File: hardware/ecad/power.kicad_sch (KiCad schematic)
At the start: 18 parts, among them J1 Conn_01x02, U1 TPS62162DSG, U2 BQ24079RGTT

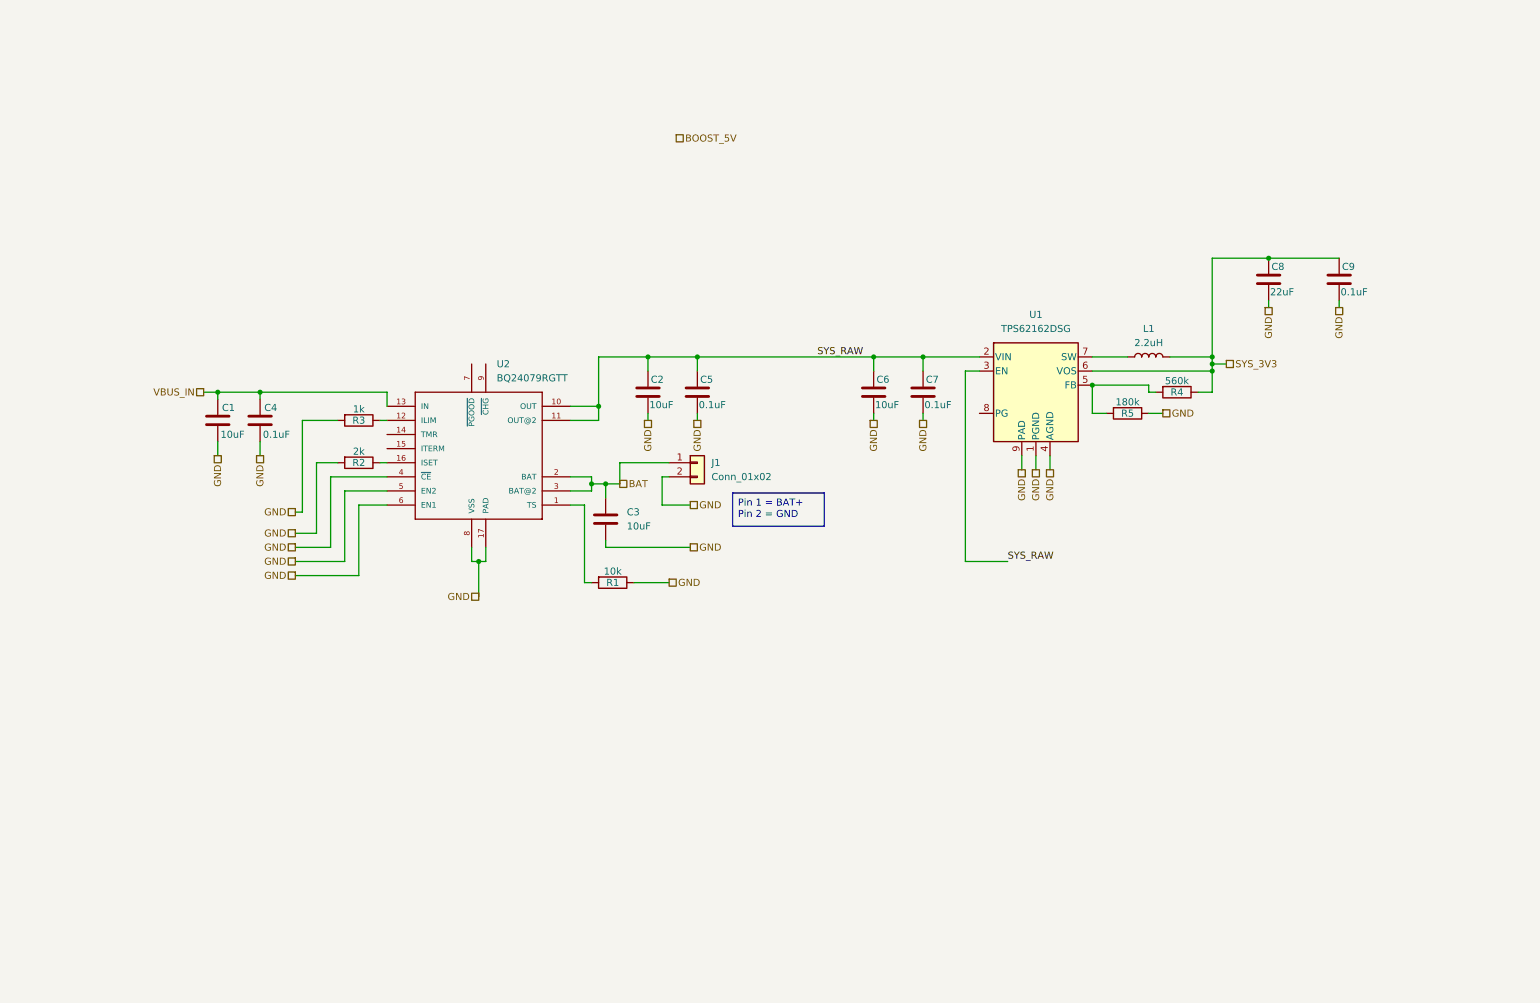
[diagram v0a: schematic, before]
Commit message: Power schematic finished, top level schematic editied to swap from I2c to SPI instead
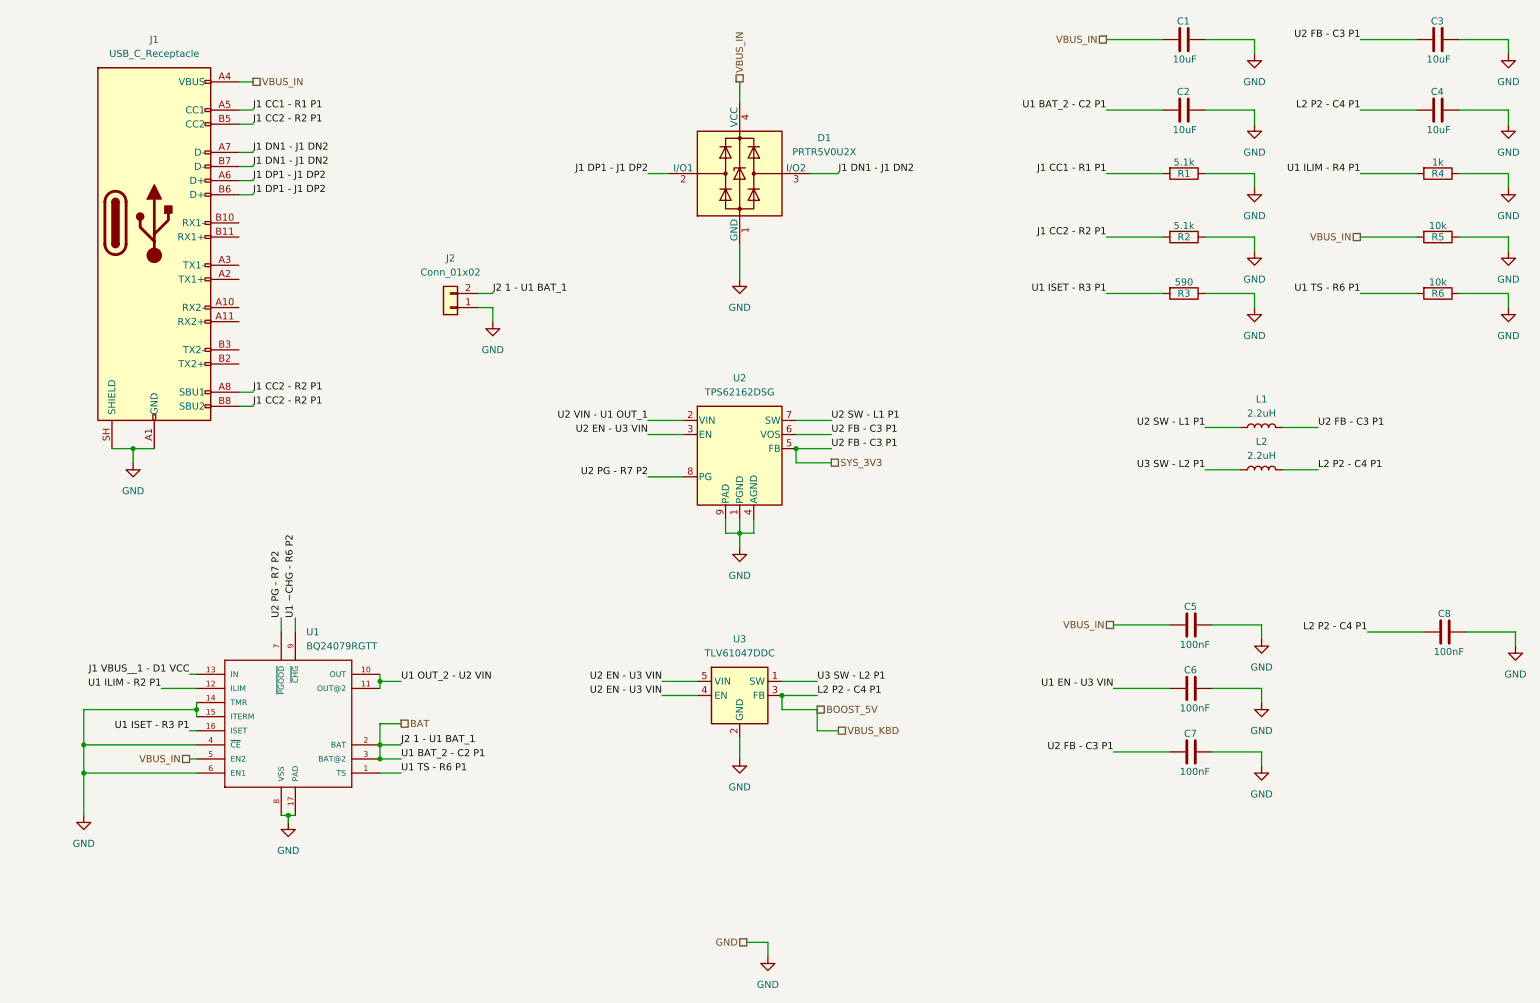
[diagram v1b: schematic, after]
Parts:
- removed C9: 0.1uF, Capacitor_SMD:C_0603_1608Metric, symbol Device:C
- removed J1: Conn_01x02, Connector_JST:JST_PH_B2B-PH-K_1x02_P2.00mm_Vertical, symbol Connector_Generic:Conn_01x02
- removed U1: TPS62162DSG, Package_SON:WSON-8-1EP_2x2mm_P0.5mm_EP0.9x1.6mm_ThermalVias, symbol Regulator_Switching:TPS62162DSG
- removed U2: BQ24079RGTT, footprints:QFN50P400X400X80-17N, symbol BQ24074RGTT:BQ24074RGTT
- added D1: PRTR5V0U2X, Package_TO_SOT_SMD:SOT-143, symbol Power_Protection:PRTR5V0U2X
- added J1: USB_C_Receptacle, Connector_USB:USB_C_Receptacle_Amphenol_12401610E4-2A_CircularHoles, symbol Connector:USB_C_Receptacle
- added J2: Conn_01x02, Connector_JST:JST_PH_B2B-PH-K_1x02_P2.00mm_Vertical, symbol Connector_Generic:Conn_01x02
- added L2: 2.2uH, Inductor_SMD:L_0603_1608Metric, symbol Device:L
- added R6: 10k, Resistor_SMD:R_0201_0603Metric, symbol Device:R
- added U1: BQ24079RGTT, footprints:QFN50P400X400X80-17N, symbol BQ24074RGTT:BQ24074RGTT
- added U2: TPS62162DSG, Package_SON:WSON-8-1EP_2x2mm_P0.5mm_EP0.9x1.6mm_ThermalVias, symbol Regulator_Switching:TPS62162DSG
- added U3: TLV61047DDC, Package_TO_SOT_SMD:SOT-23-5, symbol Regulator_Switching:TLV61047DDC
- C4: value 0.1uF -> 10uF
- C5, C7: value 0.1uF -> 100nF
- C6: value 10uF -> 100nF
- C8: value 22uF -> 100nF
- R1: value 10k -> 5.1k
- R2: value 2k -> 5.1k
- R3: value 1k -> 590
- R4: value 560k -> 1k
- R5: value 180k -> 10k
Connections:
- net SYS_RAW is gone; now on net GND: C2.1, C5.1, C6.1, C7.1
- net BAT: now also C2.2, J2.2 (Pin_2), U1.2 (BAT), U1.3 (BAT@2); no longer C3.1
- net BOOST_5V: now also C4.2, C8.2, L2.2, U3.3 (FB)
- net GND: now also C1.1, C3.1, C4.1, C8.1, R2.1, R3.1, R4.1, D1.1 (GND), J1.A1 (GND), J1.A12 (GND), J1.B1 (GND), J1.B12 (GND), J1.SH (SHIELD), J2.1 (Pin_1), R6.1, U1.14 (TMR), U1.15 (ITERM), U1.17 (PAD), U1.4 (~{CE}), U1.6 (EN1), U1.8 (VSS), U2.1 (PGND), U2.4 (AGND), U2.9 (PAD), U3.2 (GND); no longer C1.2, C2.2, C3.2, C4.2, C5.2, C6.2, C7.2, C8.2, R2.2, R3.2
- net SYS_3V3: now also C3.2, C7.2, U2.5 (FB), U2.6 (VOS); no longer C8.1, R4.1
- net VBUS_IN: now also C1.2, C5.2, R5.2, D1.4 (VCC), J1.A4 (VBUS), J1.A9 (VBUS), J1.B4 (VBUS), J1.B9 (VBUS), U1.5 (EN2); no longer C1.1, C4.1
- net J1 CC1 - R1 P1: now reaches R1.2
- net J1 CC1 - R1 P1: now also J1.A5 (CC1)
- net U1 ILIM - R4 P1: now reaches R4.2
- net U1 ILIM - R4 P1: no longer R5.2
- net U2 SW - L1 P1: now reaches L1.1
- net U2 SW - L1 P1: now also U2.7 (SW)
- new net J1 CC2 - R2 P1: J1.A8 (SBU1), J1.B5 (CC2), J1.B8 (SBU2), R2.2
- new net J1 DN1 - J1 DN2: D1.3 (I/O2), J1.A7 (D-), J1.B7 (D-)
- new net J1 DP1 - J1 DP2: D1.2 (I/O1), J1.A6 (D+), J1.B6 (D+)
- new net J1 VBUS__1 - D1 VCC: U1.13 (IN)
- new net U1 EN - U3 VIN: C6.2
- new net U1 ILIM - R2 P1: U1.12 (ILIM)
- new net U1 ISET - R3 P1: R3.2, U1.16 (ISET)
- new net U1 OUT_2 - U2 VIN: U1.10 (OUT), U1.11 (OUT@2)
- new net U1 TS - R6 P1: R6.2, U1.1 (TS)
- new net U1 ~CHG - R6 P2: U1.9 (~{CHG})
- new net U2 EN - U3 VIN: U2.3 (EN), U3.4 (EN), U3.5 (VIN)
- new net U2 PG - R7 P2: U1.7 (~{PGOOD}), U2.8 (PG)
- new net U2 VIN - U1 OUT_1: U2.2 (VIN)
- new net U3 SW - L2 P1: L2.1, U3.1 (SW)

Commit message: finsihed 6/7 sheets, usb_data needs work. Some warnings to be dealt with aswell but no hard errors.
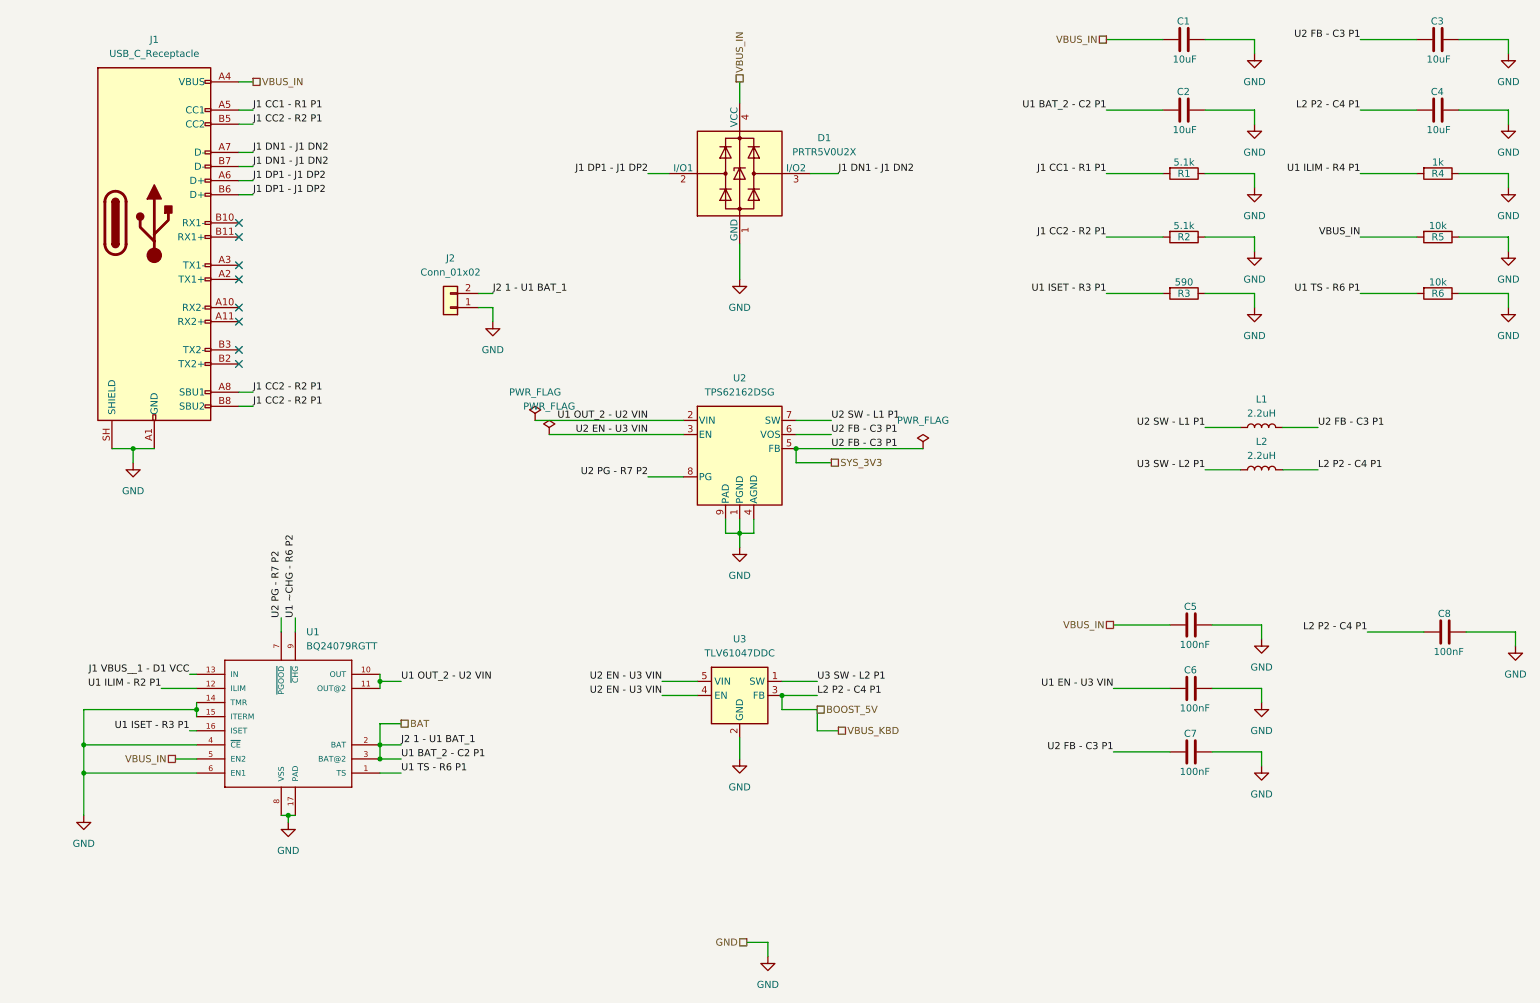
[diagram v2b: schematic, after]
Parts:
- U1: MP BQ24074RGTT -> BQ24079RGTT
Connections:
- net U2 VIN - U1 OUT_1 is gone; now on net U1 OUT_2 - U2 VIN: U2.2 (VIN)
- no-connect marks 0 -> 8
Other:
- company: avega systems -> āvega systems

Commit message: Updated schematics to get rid of errors and warnings
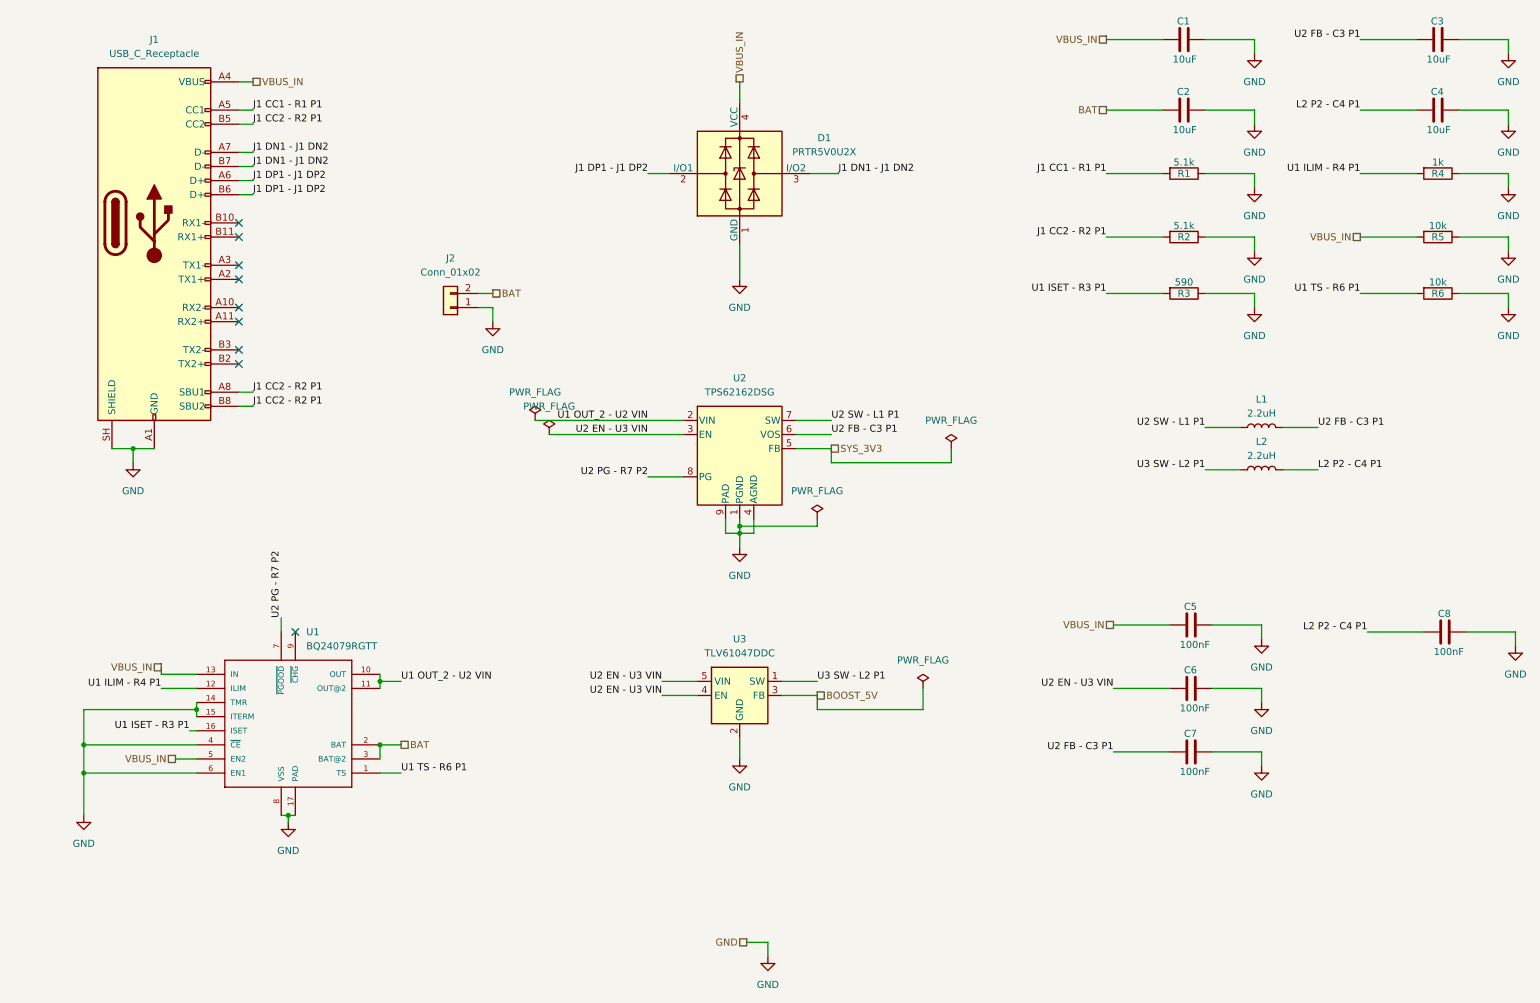
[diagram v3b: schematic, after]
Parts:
- U1: footprint footprints:QFN50P400X400X80-17N -> Package_DFN_QFN:VQFN-16-1EP_3x3mm_P0.5mm_EP1.68x1.68mm_ThermalVias; MP BQ24079RGTT -> BQ24074RGTT
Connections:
- net J1 VBUS__1 - D1 VCC is gone; now on net VBUS_IN: U1.13 (IN)
- net U1 EN - U3 VIN is gone; now on net U2 EN - U3 VIN: C6.2
- net U1 ILIM - R2 P1 is gone; now on net U1 ILIM - R4 P1: U1.12 (ILIM)
- net BOOST_5V: no longer C4.2, C8.2, L2.2
- net SYS_3V3: no longer C3.2, C7.2, L1.2, U2.6 (VOS)
- net U1 ~CHG - R6 P2: no longer names the net of U1.9 (~{CHG})
- new net L2 P2 - C4 P1: C4.2, C8.2, L2.2
- new net U2 FB - C3 P1: C3.2, C7.2, L1.2, U2.6 (VOS)
- no-connect marks 8 -> 9
